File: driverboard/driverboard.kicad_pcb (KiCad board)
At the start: 2 copper layers, 47 x 48.3 mm, 25 parts, among them IC1 NCV7240ADPR2G, J1 valve 1, J10 data output, J11 12V input, J12 12V output, J2 valve 2, J3 valve 3, J4 valve 4, J5 valve 5, J6 valve 6, J7 valve 7, J8 valve 8, J9 data input, U1 74LVC1G34

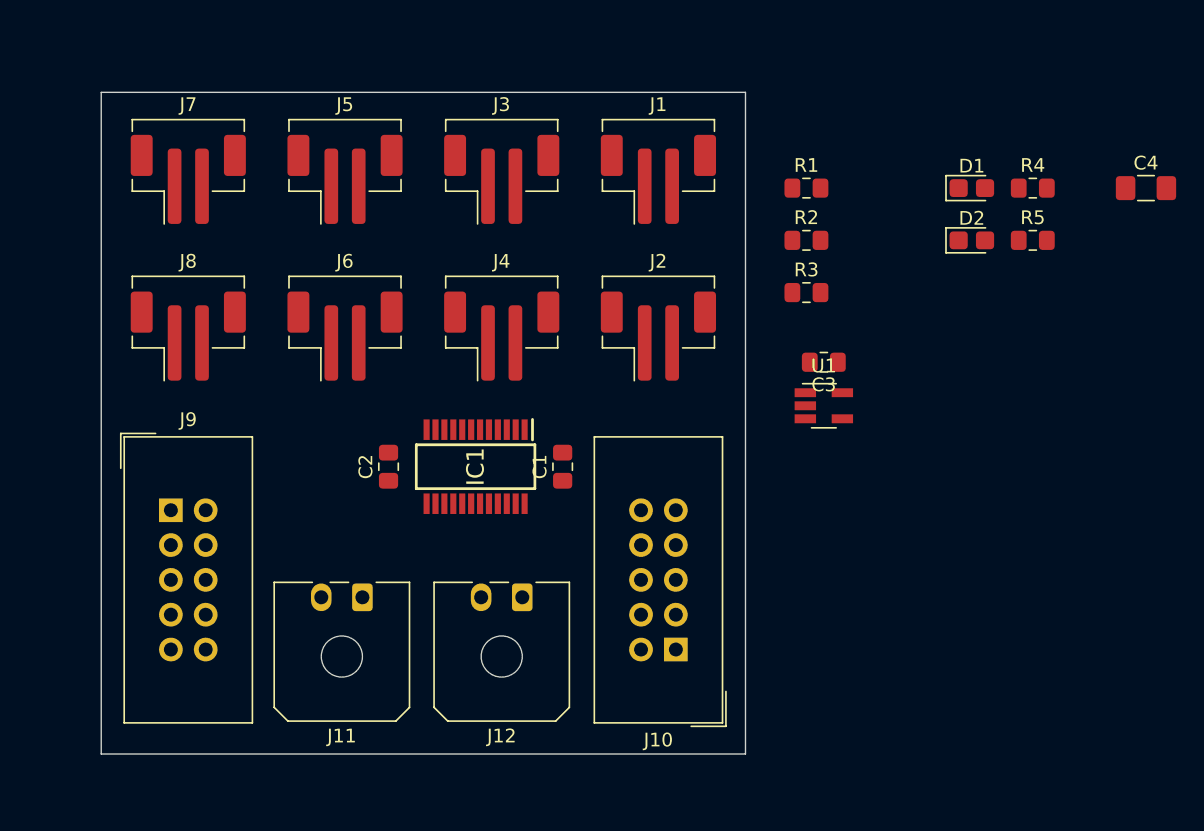
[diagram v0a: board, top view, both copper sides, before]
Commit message: route output traces
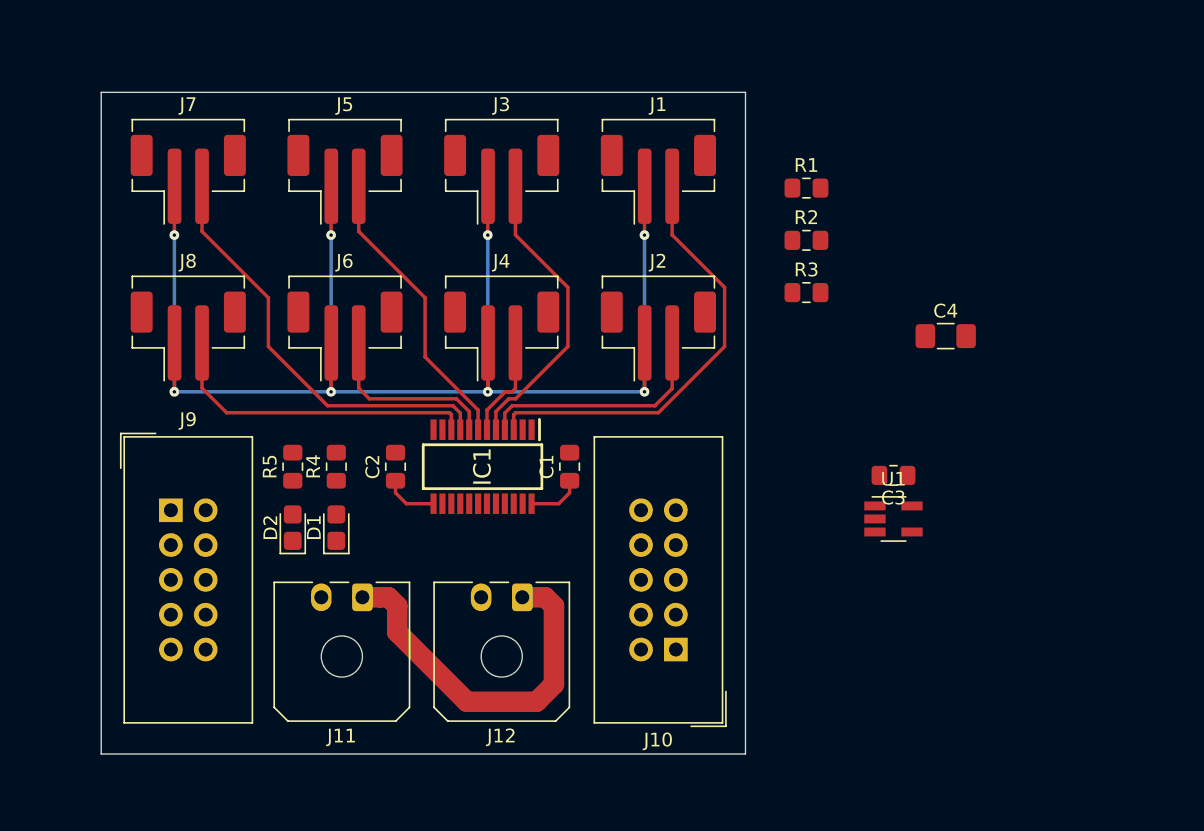
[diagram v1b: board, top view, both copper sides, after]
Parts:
- moved R5 56.4 mm to (63.5, 164.5), turned to 90 degrees
- moved R4 54.7 mm to (66.7, 164.5), turned to 90 degrees
- moved D2 53.8 mm to (63.5, 168.9), turned to 90 degrees
- moved D1 52.6 mm to (66.7, 168.9), turned to 90 degrees
- moved C4 18.2 mm to (111.1, 154.9)
- moved C3 9.69 mm to (107.3, 165.1)
- moved U1 9.69 mm to (107.3, 168.3)
- moved IC1 0.51 mm to (77.3, 164.5)
- moved C1 0.51 mm to (83.7, 164.5)
- moved C2 0.51 mm to (71.0, 164.5)
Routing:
- net +12V: track 0.00 -> 135.5 mm, vias 0 -> 8
- net Net-(IC1-Pad3): track 0.00 -> 31.8 mm
- net Net-(IC1-Pad9): track 0.00 -> 30.9 mm
- net Net-(IC1-Pad10): track 0.00 -> 23.4 mm
- net Net-(IC1-Pad5): track 0.00 -> 21.8 mm
- net Net-(IC1-Pad7): track 0.00 -> 21.4 mm
- net Net-(IC1-Pad4): track 0.00 -> 17.5 mm
- net Net-(IC1-Pad8): track 0.00 -> 13.4 mm
- net Net-(IC1-Pad6): track 0.00 -> 7.48 mm
- net VCC: track 0.00 -> 3.98 mm
- net +5V: track 0.00 -> 3.98 mm
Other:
- net class Default: clearance 0.2 -> 0.1524; trace_width 0.25 -> 0.1524; via_dia 0.8 -> 0.508; via_drill 0.4 -> 0.254
- net class Drive added: clearance 0.1524, trace_width 0.254, via_dia 0.7112, via_drill 0.254
- net class Power added: clearance 0.1524, trace_width 1.4986, via_dia 0.508, via_drill 0.254
- rule pad_to_mask_clearance: 0.051 -> 0.0508
- rule solder_mask_min_width: 0.25 -> 0.1016
- rule trace_clearance: 0.2 -> 0.1524

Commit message: start routing data connectors
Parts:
- moved C3 44.4 mm to (63.2, 170.2)
- moved R3 41.0 mm to (63.2, 167.9), turned to 180 degrees
- moved U1 39.2 mm to (68.1, 168.9), turned to 180 degrees
- moved R2 35.6 mm to (72.9, 169.9), turned to 180 degrees
- moved R1 35.1 mm to (77.2, 169.9)
- moved C4 11.3 mm to (99.8, 155.4)
- moved D1 5.66 mm to (67.6, 163.3), turned to 0 degrees
- moved D2 5.24 mm to (67.6, 165.6), turned to 0 degrees
- moved R4 3.61 mm to (63.2, 163.3), turned to 180 degrees
- moved J9 1.78 mm to (54.6, 169.4)
- moved J10 1.78 mm to (91.4, 179.6)
- moved J11 1.78 mm to (68.6, 175.8)
- moved J12 1.78 mm to (80.2, 175.8)
- moved R5 1.17 mm to (63.2, 165.6), turned to 180 degrees
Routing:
- net Net-(IC1-Pad23): track 0.00 -> 39.9 mm
- net Net-(J10-Pad7): track 0.00 -> 27.5 mm
- net Net-(IC1-Pad22): track 0.00 -> 21.9 mm
- net Net-(IC1-Pad21): track 0.00 -> 21.3 mm
- net Net-(IC1-Pad20): track 0.00 -> 14.8 mm
- net Net-(J9-Pad5): track 0.00 -> 13.9 mm
- net Net-(IC1-Pad19): track 0.00 -> 3.00 mm
- net Net-(J10-Pad5): track 0.00 -> 2.87 mm
- net VCC: track 3.98 -> 6.57 mm
- net Net-(R3-Pad1): track 0.00 -> 2.48 mm
- net Net-(D2-Pad1): track 0.00 -> 2.33 mm
- net Net-(D1-Pad1): track 0.00 -> 2.33 mm
- net +12V: track 135.5 -> 137.4 mm, vias 8 -> 9

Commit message: finish routing signals
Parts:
- moved C4 46.8 mm to (53.3, 160.8), turned to 180 degrees
- moved J9 1.02 mm to (54.6, 168.4)
- moved J10 1.02 mm to (91.4, 178.6)
- moved J11 1.02 mm to (68.6, 174.8)
- moved J12 1.02 mm to (80.2, 174.8)
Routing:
- net Net-(IC1-Pad20): track 14.8 -> 40.7 mm, vias 0 -> 2
- net Net-(J10-Pad5): track 2.87 -> 25.3 mm, vias 0 -> 1
- net Net-(IC1-Pad21): track 21.3 -> 39.5 mm, vias 0 -> 1
- net Net-(IC1-Pad23): track 39.9 -> 57.4 mm, vias 0 -> 1
- net +12V: track 137.4 -> 152.4 mm
- net Net-(IC1-Pad22): track 21.9 -> 33.2 mm
- net Net-(J10-Pad7): track 27.5 -> 19.3 mm, vias 0 -> 1
- net Net-(J9-Pad5): track 13.9 -> 11.0 mm

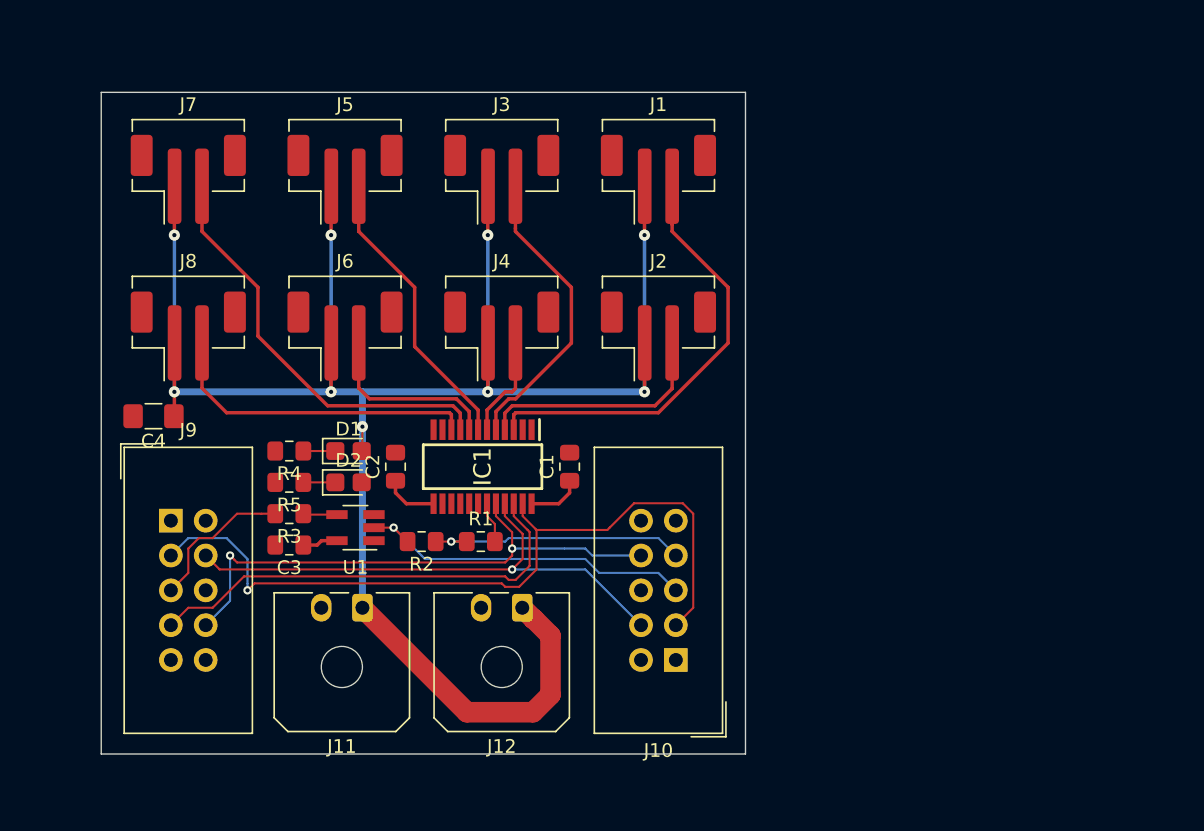
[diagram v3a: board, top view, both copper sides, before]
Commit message: add ground polygon fill
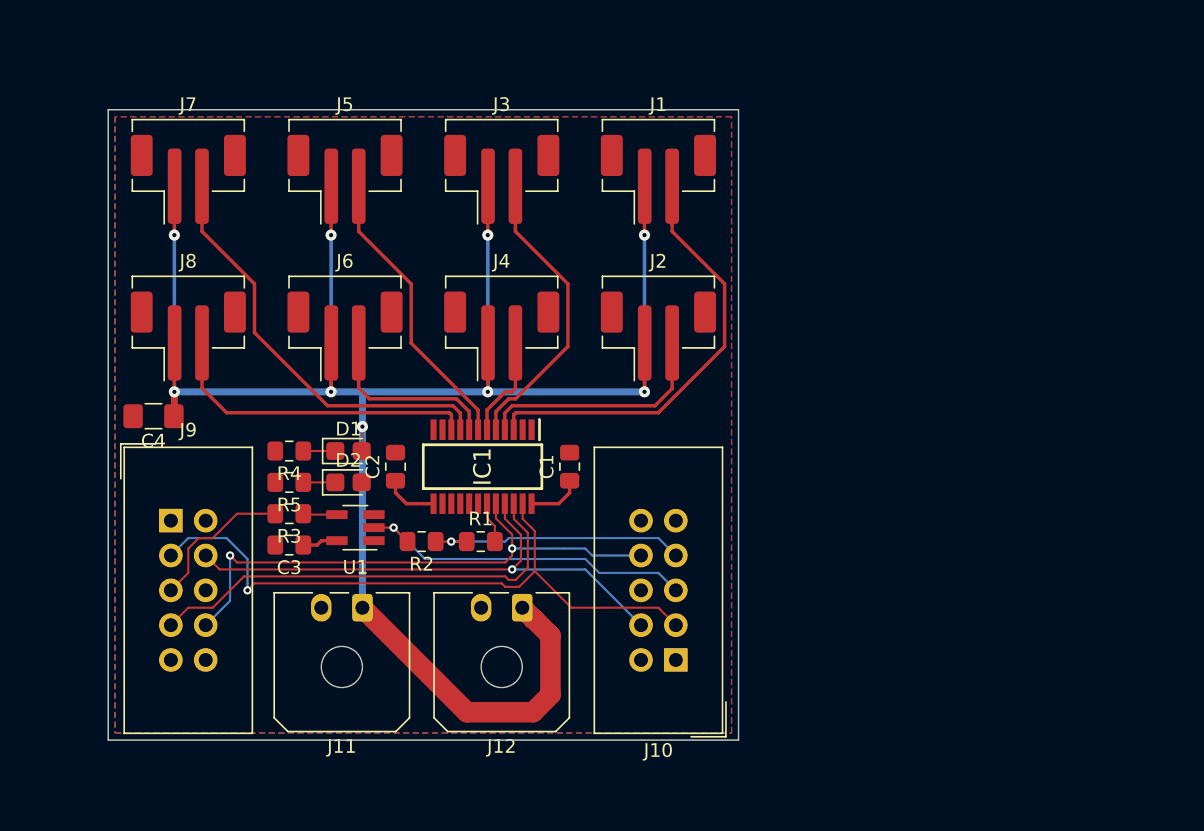
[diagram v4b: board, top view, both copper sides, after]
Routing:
- net Net-(IC1-Pad23): track 57.4 -> 48.0 mm
- added copper zone on B.Cu, net GND
- added copper zone on F.Cu, net GND
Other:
- board size 47 x 48.3 mm -> 46 x 46 mm

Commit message: finish routing
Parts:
- D1: value green -> yellow
- turned D1 to 180 degrees
- turned D2 to 180 degrees
- turned R4 to 0 degrees
- turned R5 to 0 degrees
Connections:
- D1 pad 1: Net-(D1-Pad1) -> GND
- D1 pad 2: +12V -> Net-(D1-Pad2)
- D2 pad 1: Net-(D2-Pad1) -> GND
- D2 pad 2: +5V -> Net-(D2-Pad2)
- J12 pad 1: +12V -> GND
- J12 pad 2: GND -> +12V
- R4 pad 1: Net-(D1-Pad1) -> +12V
- R4 pad 2: GND -> Net-(D1-Pad2)
- R5 pad 1: Net-(D2-Pad1) -> +5V
- R5 pad 2: GND -> Net-(D2-Pad2)
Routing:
- net +5V: track 3.98 -> 83.3 mm
- net VCC: track 6.57 -> 81.2 mm
- net +12V: track 152.4 -> 143.1 mm, vias 9 -> 8
- net GND: track 0.00 -> 3.36 mm, vias 0 -> 13
- net Net-(D2-Pad2): track 0.00 -> 2.33 mm
- net Net-(D2-Pad1): track 2.33 -> 0.00 mm
- net Net-(D1-Pad2): track 0.00 -> 2.33 mm
- net Net-(D1-Pad1): track 2.33 -> 0.00 mm
- net Net-(J10-Pad5): track 25.3 -> 26.8 mm
- net Net-(IC1-Pad23): track 48.0 -> 48.1 mm, vias 1 -> 2

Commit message: improve routing
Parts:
- turned C3 to 0 degrees
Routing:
- net +12V: track 143.1 -> 151.0 mm, vias 8 -> 9
- net VCC: track 81.2 -> 83.3 mm
- net +5V: track 83.3 -> 84.5 mm
- net GND: vias 13 -> 21

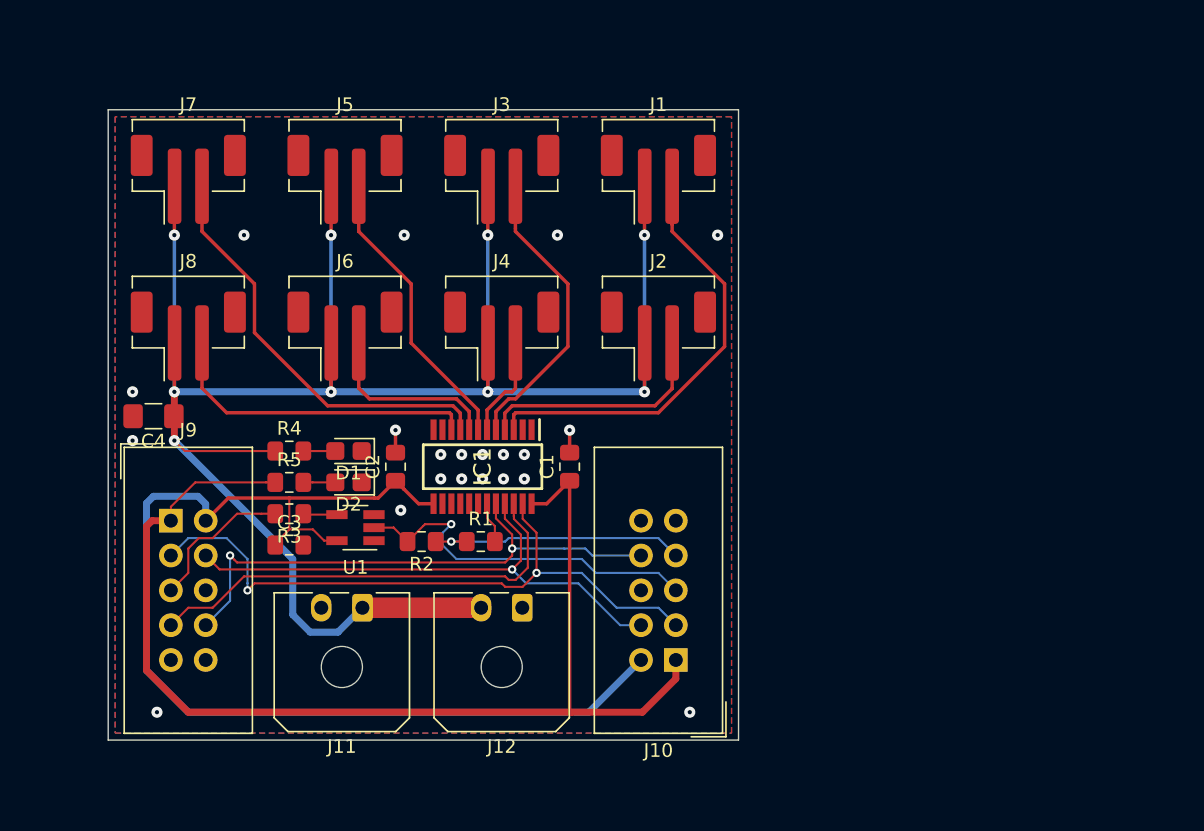
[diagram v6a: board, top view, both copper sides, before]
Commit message: add reverse polarity protection
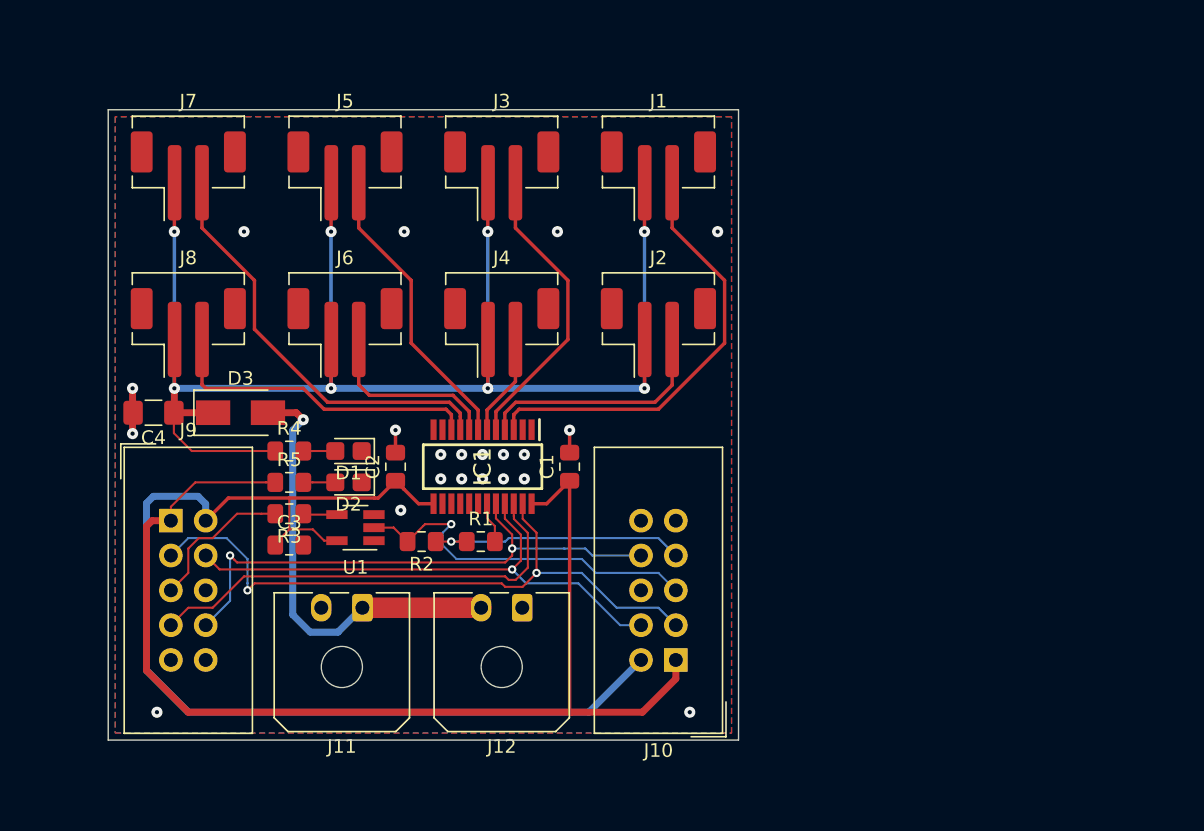
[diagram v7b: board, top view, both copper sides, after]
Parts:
- added D3: MBRA340, Diode_SMD:D_SMA, F.Cu at (59.7, 160.5)
- moved C4 0.25 mm to (53.3, 160.5)
- moved J1 0.25 mm to (90.2, 143.3)
- moved J2 0.25 mm to (90.2, 154.7)
- moved J3 0.25 mm to (78.7, 143.3)
- moved J4 0.25 mm to (78.7, 154.7)
- moved J5 0.25 mm to (67.3, 143.3)
- moved J6 0.25 mm to (67.3, 154.7)
- moved J7 0.25 mm to (55.9, 143.3)
- moved J8 0.25 mm to (55.9, 154.7)
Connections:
- J11 pad 1: +12V -> Net-(D3-Pad2)
- J12 pad 2: +12V -> Net-(D3-Pad2)
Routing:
- net Net-(D3-Pad2): track 0.00 -> 32.3 mm, vias 0 -> 1
- net +12V: track 151.0 -> 122.6 mm, vias 9 -> 8
- net GND: track 3.36 -> 6.41 mm
